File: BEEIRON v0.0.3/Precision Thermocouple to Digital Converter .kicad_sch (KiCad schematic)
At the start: 17 parts, among them U6 MAX31856

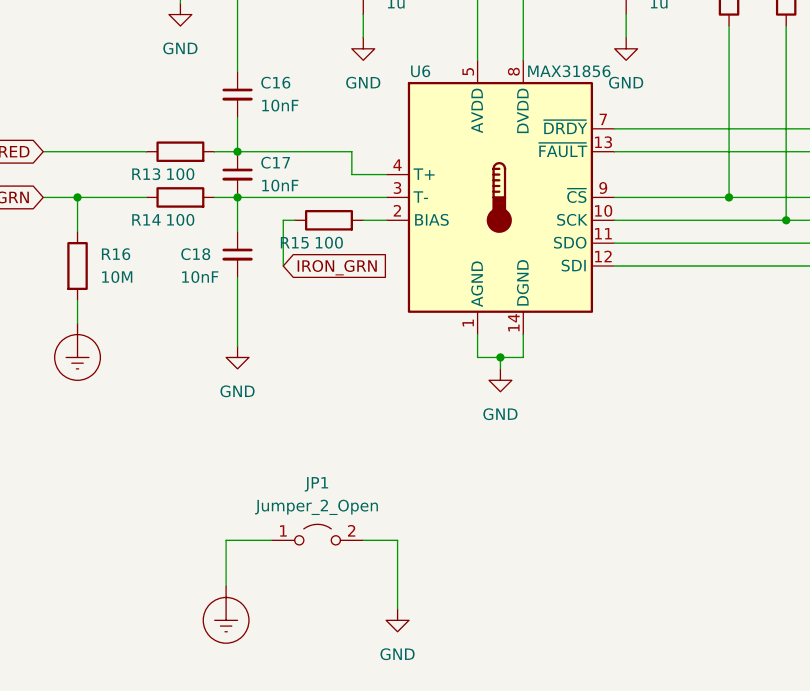
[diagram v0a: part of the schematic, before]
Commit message: minor edit in the schematics
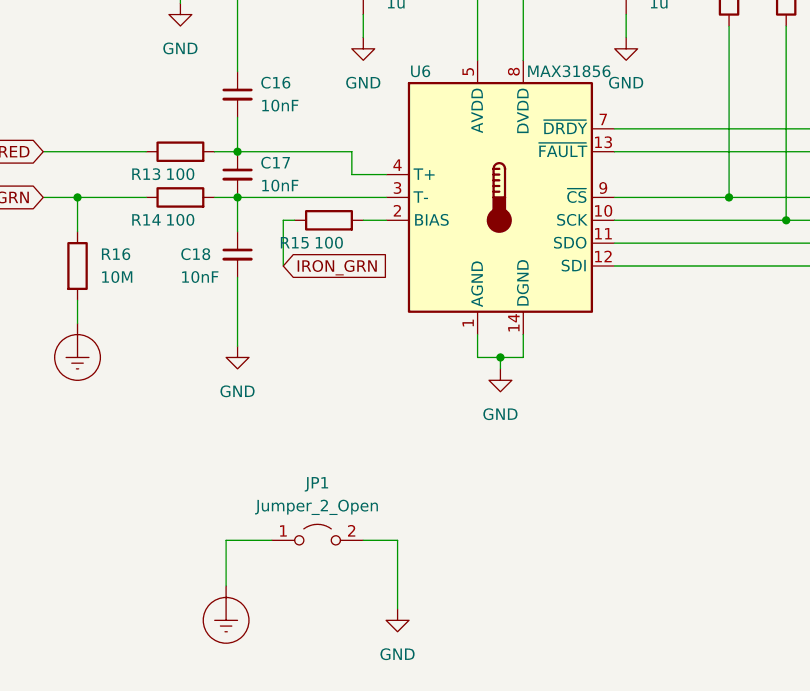
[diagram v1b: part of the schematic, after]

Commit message: added bakup file
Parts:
- removed D3, D4, D5: 1N4148W, Diode_SMD:D_SOD-123, symbol Diode:1N4148W
- removed R10, R11, R12: 10K, Resistor_SMD:R_0805_2012Metric, symbol Device:R
- added JP1, JP2, JP3, JP4, JP5, JP6: Jumper_2_Open, Jumper:SolderJumper-2_P1.3mm_Open_TrianglePad1.0x1.5mm, symbol Jumper:Jumper_2_Open
- added Q1, Q2, Q3, Q4, Q5, Q6: BSS138, Package_TO_SOT_SMD:SOT-23, symbol Transistor_FET:BSS138
- added R14, R16, R18, R20, R22, R24: 10K, Resistor_SMD:R_0805_2012Metric, symbol Device:R
- added R15, R17, R19, R21, R23, R25: K10K, Resistor_SMD:R_0805_2012Metric, symbol Device:R
- renumbered JP1 to JP7, R13 to R10, R14 to R11, R15 to R12, R16 to R13
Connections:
- net +3V3: now also Q1.1 (G), Q2.1 (G), Q3.1 (G), Q4.1 (G), Q5.1 (G), Q6.1 (G), R14.2, R16.2, R18.2, R20.2, R22.2, R24.2
- net D10/CS: now also JP3.2 (B), Q1.3 (D), R15.1
- net D11/SDI: now also JP6.2 (B), Q2.3 (D), R17.1
- net D12/SDO: now also JP5.2 (B), Q5.3 (D), R23.1; no longer U6.11 (SDO)
- net D13/SCK: now also JP4.2 (B), Q6.3 (D), R25.1
- net D6/FAULT: now also JP2.2 (B), Q4.3 (D), R21.1; no longer U6.13 (~{FAULT})
- net D7/DDRY: now also JP1.2 (B), Q3.3 (D), R19.1; no longer U6.7 (~{DRDY})
- net CS: now reaches U6.9 (~{CS})
- net CS: now also JP3.1 (A), Q1.2 (S), R14.1
- net SCK: now reaches U6.10 (SCK)
- net SCK: now also JP4.1 (A), Q6.2 (S), R24.1
- net SDI: now reaches U6.12 (SDI)
- net SDI: now also JP6.1 (A), Q2.2 (S), R16.1
- new net +5V: R15.2, R17.2, R19.2, R21.2, R23.2, R25.2
- new net DDRY: JP1.1 (A), Q3.2 (S), R18.1, U6.7 (~{DRDY})
- new net FAULT: JP2.1 (A), Q4.2 (S), R20.1, U6.13 (~{FAULT})
- new net SDO: JP5.1 (A), Q5.2 (S), R22.1, U6.11 (SDO)
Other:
- moved on the sheet: C14, C15, C16, C17, C18, JP7, R10, R11, R12, R13, U6
